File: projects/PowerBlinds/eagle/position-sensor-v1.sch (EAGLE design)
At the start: 22 parts, among them Q1 MAX481SO08, U1 ACS712ELCTR-20A-T

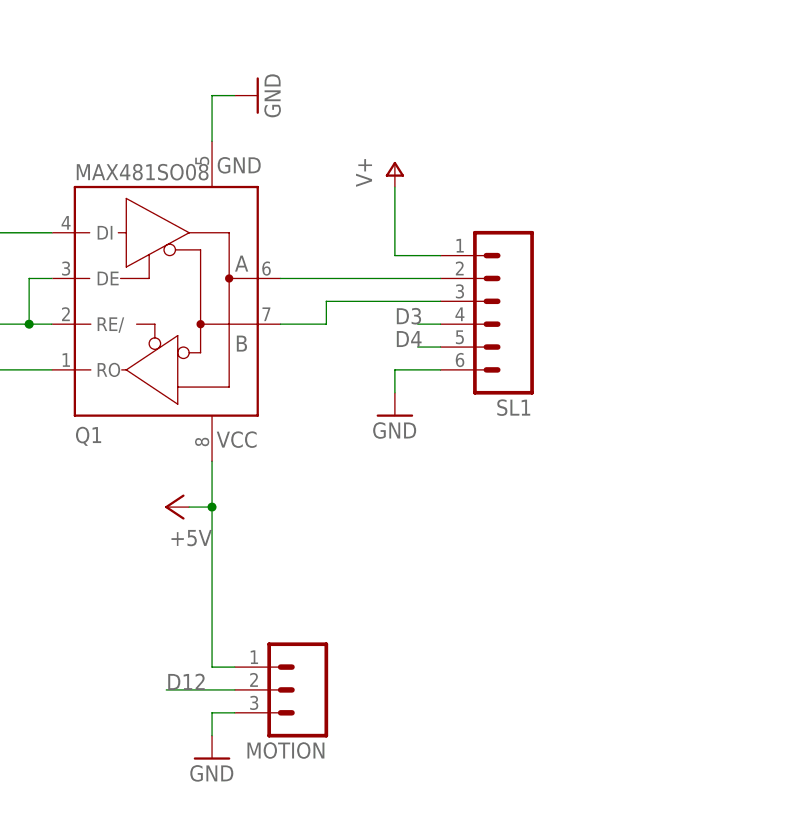
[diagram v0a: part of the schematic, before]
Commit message: Power blinds: adding external pull-up resistors for inputs, and adding TVS diode for RS-485
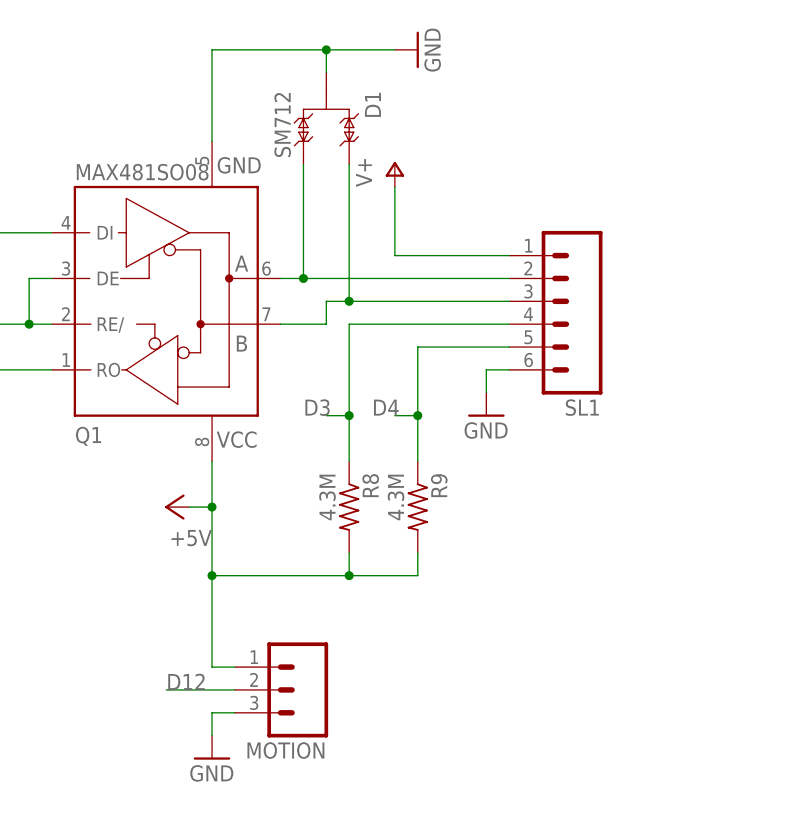
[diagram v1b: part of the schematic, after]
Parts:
- added D1: SM712, serge:SM712
- added R8, R9: 4.3M, adafruit:R-US_R0603
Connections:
- net +5V: now also R8.2, R9.2
- net D3: now also R8.1
- net D4: now also R9.1
- net GND: now also D1.3
- net N$1: now also D1.1
- net N$2: now also D1.2
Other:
- moved on the sheet: SL1
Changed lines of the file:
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@@
 <part name="F1" library="adafruit" deviceset="PTCFUSE" device="-1812"/>
 <part name="SL1" library="con-amp-quick" deviceset="M06" device=""/>
+<part name="R8" library="adafruit" deviceset="R-US_" device="R0603" value="4.3M"/>
+<part name="R9" library="adafruit" deviceset="R-US_" device="R0603" value="4.3M"/>
+<part name="D1" library="serge" deviceset="SM712" device=""/>
 </parts>
 <sheets>
@@
 <instance part="U$1" gate="G$1" x="15.24" y="76.2"/>
 <instance part="Q1" gate="G$1" x="114.3" y="132.08" rot="MR180"/>
-<instance part="GND1" gate="1" x="139.7" y="119.38"/>
-<instance part="GND2" gate="1" x="124.46" y="154.94" rot="R90"/>
+<instance part="GND1" gate="1" x="149.86" y="119.38"/>
+<instance part="GND2" gate="1" x="142.24" y="160.02" rot="R90"/>
 <instance part="P+2" gate="1" x="114.3" y="109.22" rot="R90"/>
 <instance part="P+4" gate="1" x="139.7" y="147.32"/>
@@
 <instance part="P+9" gate="1" x="101.6" y="22.86"/>
 <instance part="F1" gate="G$1" x="213.36" y="10.16" rot="R90"/>
-<instance part="SL1" gate="G$1" x="149.86" y="132.08" rot="R180"/>
+<instance part="SL1" gate="G$1" x="157.48" y="132.08" rot="R180"/>
+<instance part="R8" gate="G$1" x="134.62" y="109.22" rot="R270"/>
+<instance part="R9" gate="G$1" x="142.24" y="109.22" rot="R270"/>
+<instance part="D1" gate="G$1" x="132.08" y="152.4" rot="R180"/>
 </instances>
 <busses>
@@
 <segment>
 <pinref part="Q1" gate="G$1" pin="A"/>
-<wire x1="144.78" y1="134.62" x2="127" y2="134.62" width="0.1524" layer="91"/>
+<wire x1="152.4" y1="134.62" x2="129.54" y2="134.62" width="0.1524" layer="91"/>
 <pinref part="SL1" gate="G$1" pin="2"/>
+<pinref part="D1" gate="G$1" pin="1"/>
+<wire x1="129.54" y1="134.62" x2="127" y2="134.62" width="0.1524" layer="91"/>
+<wire x1="129.54" y1="147.32" x2="129.54" y2="134.62" width="0.1524" layer="91"/>
+<junction x="129.54" y="134.62"/>
 </segment>
 </net>
 <net name="N$2" class="0">
 <segment>
-<wire x1="144.78" y1="132.08" x2="132.08" y2="132.08" width="0.1524" layer="91"/>
+<wire x1="152.4" y1="132.08" x2="134.62" y2="132.08" width="0.1524" layer="91"/>
+<wire x1="134.62" y1="132.08" x2="132.08" y2="132.08" width="0.1524" layer="91"/>
 <wire x1="132.08" y1="132.08" x2="132.08" y2="129.54" width="0.1524" layer="91"/>
 <pinref part="Q1" gate="G$1" pin="B"/>
+<pinref part="SL1" gate="G$1" pin="3"/>
 <wire x1="132.08" y1="129.54" x2="127" y2="129.54" width="0.1524" layer="91"/>
-<pinref part="SL1" gate="G$1" pin="3"/>
+<pinref part="D1" gate="G$1" pin="2"/>
+<wire x1="134.62" y1="147.32" x2="134.62" y2="132.08" width="0.1524" layer="91"/>
+<junction x="134.62" y="132.08"/>
 </segment>
 </net>
 <net name="GND" class="0">
 <segment>
-<wire x1="144.78" y1="124.46" x2="139.7" y2="124.46" width="0.1524" layer="91"/>
-<wire x1="139.7" y1="124.46" x2="139.7" y2="121.92" width="0.1524" layer="91"/>
+<wire x1="152.4" y1="124.46" x2="149.86" y2="124.46" width="0.1524" layer="91"/>
+<wire x1="149.86" y1="124.46" x2="149.86" y2="121.92" width="0.1524" layer="91"/>
 <pinref part="GND1" gate="1" pin="GND"/>
 <pinref part="SL1" gate="G$1" pin="6"/>
@@
 <segment>
 <pinref part="Q1" gate="G$1" pin="GND"/>
-<wire x1="119.38" y1="149.86" x2="119.38" y2="154.94" width="0.1524" layer="91"/>
+<wire x1="119.38" y1="149.86" x2="119.38" y2="160.02" width="0.1524" layer="91"/>
 <pinref part="GND2" gate="1" pin="GND"/>
-<wire x1="119.38" y1="154.94" x2="121.92" y2="154.94" width="0.1524" layer="91"/>
+<wire x1="119.38" y1="160.02" x2="132.08" y2="160.02" width="0.1524" layer="91"/>
+<pinref part="D1" gate="G$1" pin="3"/>
+<wire x1="132.08" y1="160.02" x2="139.7" y2="160.02" width="0.1524" layer="91"/>
+<wire x1="132.08" y1="157.48" x2="132.08" y2="160.02" width="0.1524" layer="91"/>
+<junction x="132.08" y="160.02"/>
 </segment>
 <segment>
@@
 <pinref part="P+4" gate="1" pin="V+"/>
 <pinref part="SL1" gate="G$1" pin="1"/>
-<wire x1="139.7" y1="137.16" x2="144.78" y2="137.16" width="0.1524" layer="91"/>
+<wire x1="139.7" y1="137.16" x2="152.4" y2="137.16" width="0.1524" layer="91"/>
 </segment>
 <segment>
@@
 <pinref part="MOTION" gate="G$1" pin="1"/>
 <wire x1="121.92" y1="91.44" x2="119.38" y2="91.44" width="0.1524" layer="91"/>
-<wire x1="119.38" y1="91.44" x2="119.38" y2="109.22" width="0.1524" layer="91"/>
+<wire x1="119.38" y1="91.44" x2="119.38" y2="101.6" width="0.1524" layer="91"/>
 <junction x="119.38" y="109.22"/>
+<pinref part="R9" gate="G$1" pin="2"/>
+<wire x1="119.38" y1="101.6" x2="119.38" y2="109.22" width="0.1524" layer="91"/>
+<wire x1="142.24" y1="104.14" x2="142.24" y2="101.6" width="0.1524" layer="91"/>
+<wire x1="142.24" y1="101.6" x2="134.62" y2="101.6" width="0.1524" layer="91"/>
+<junction x="119.38" y="101.6"/>
+<pinref part="R8" gate="G$1" pin="2"/>
+<wire x1="134.62" y1="101.6" x2="119.38" y2="101.6" width="0.1524" layer="91"/>
+<wire x1="134.62" y1="104.14" x2="134.62" y2="101.6" width="0.1524" layer="91"/>
+<junction x="134.62" y="101.6"/>
 </segment>
 <segment>
@@
 <segment>
 <pinref part="SL1" gate="G$1" pin="5"/>
-<wire x1="144.78" y1="127" x2="142.24" y2="127" width="0.1524" layer="91"/>
-<label x="139.7" y="127" size="1.778" layer="95"/>
+<wire x1="152.4" y1="127" x2="142.24" y2="127" width="0.1524" layer="91"/>
+<label x="137.16" y="119.38" size="1.778" layer="95"/>
+<pinref part="R9" gate="G$1" pin="1"/>
+<wire x1="142.24" y1="127" x2="142.24" y2="119.38" width="0.1524" layer="91"/>
+<wire x1="142.24" y1="119.38" x2="142.24" y2="114.3" width="0.1524" layer="91"/>
+<wire x1="142.24" y1="119.38" x2="139.7" y2="119.38" width="0.1524" layer="91"/>
+<junction x="142.24" y="119.38"/>
 </segment>
 </net>
@@
 <segment>
 <pinref part="SL1" gate="G$1" pin="4"/>
-<wire x1="144.78" y1="129.54" x2="142.24" y2="129.54" width="0.1524" layer="91"/>
-<label x="139.7" y="129.54" size="1.778" layer="95"/>
-</segment>
-</net>
+<wire x1="152.4" y1="129.54" x2="134.62" y2="129.54" width="0.1524" layer="91"/>
+<label x="129.54" y="119.38" size="1.778" layer="95"/>
+<wire x1="134.62" y1="129.54" x2="134.62" y2="119.38" width="0.1524" layer="91"/>
+<pinref part="R8" gate="G$1" pin="1"/>
+<wire x1="134.62" y1="119.38" x2="134.62" y2="114.3" width="0.1524" layer="91"/>
+<wire x1="134.62" y1="119.38" x2="132.08" y2="119.38" width="0.1524" layer="91"/>
+<junction x="134.62" y="119.38"/>
+</segment>
+</net>
